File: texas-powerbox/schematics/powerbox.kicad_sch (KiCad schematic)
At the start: 32 parts, among them J1 BATTERY, J2 ADAPTER, J3 USB_STACKED, J4 USB_STACKED, J7 5V, J8 24V, K1 J107F1CS1224VDC.36, Q1 AOD417, U1 TPS54331GDR

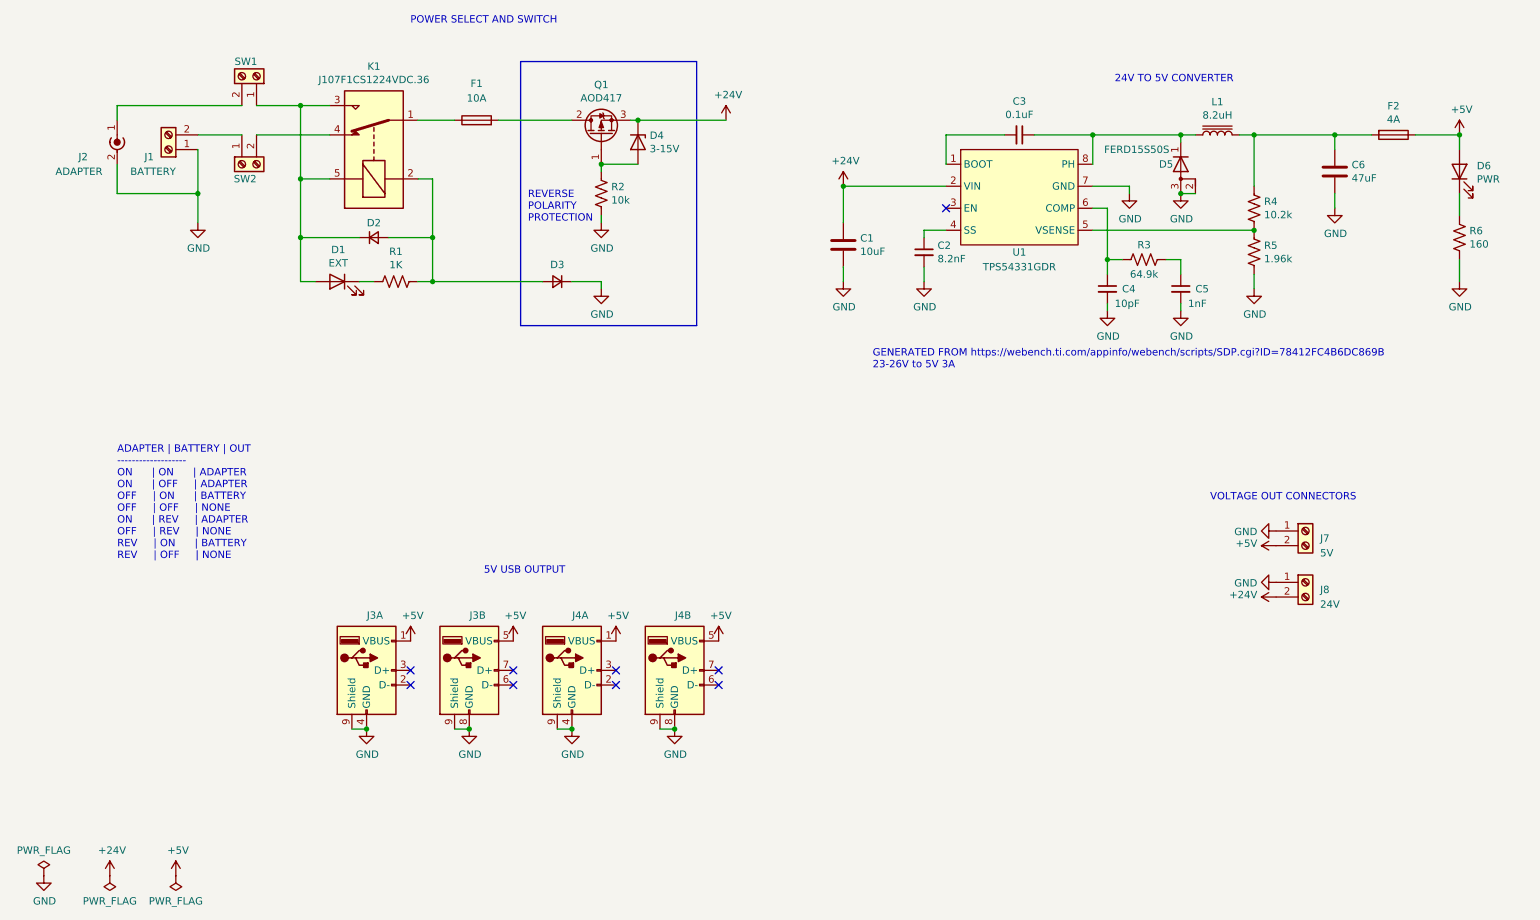
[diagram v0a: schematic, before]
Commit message: updated to use alternative bulk converter
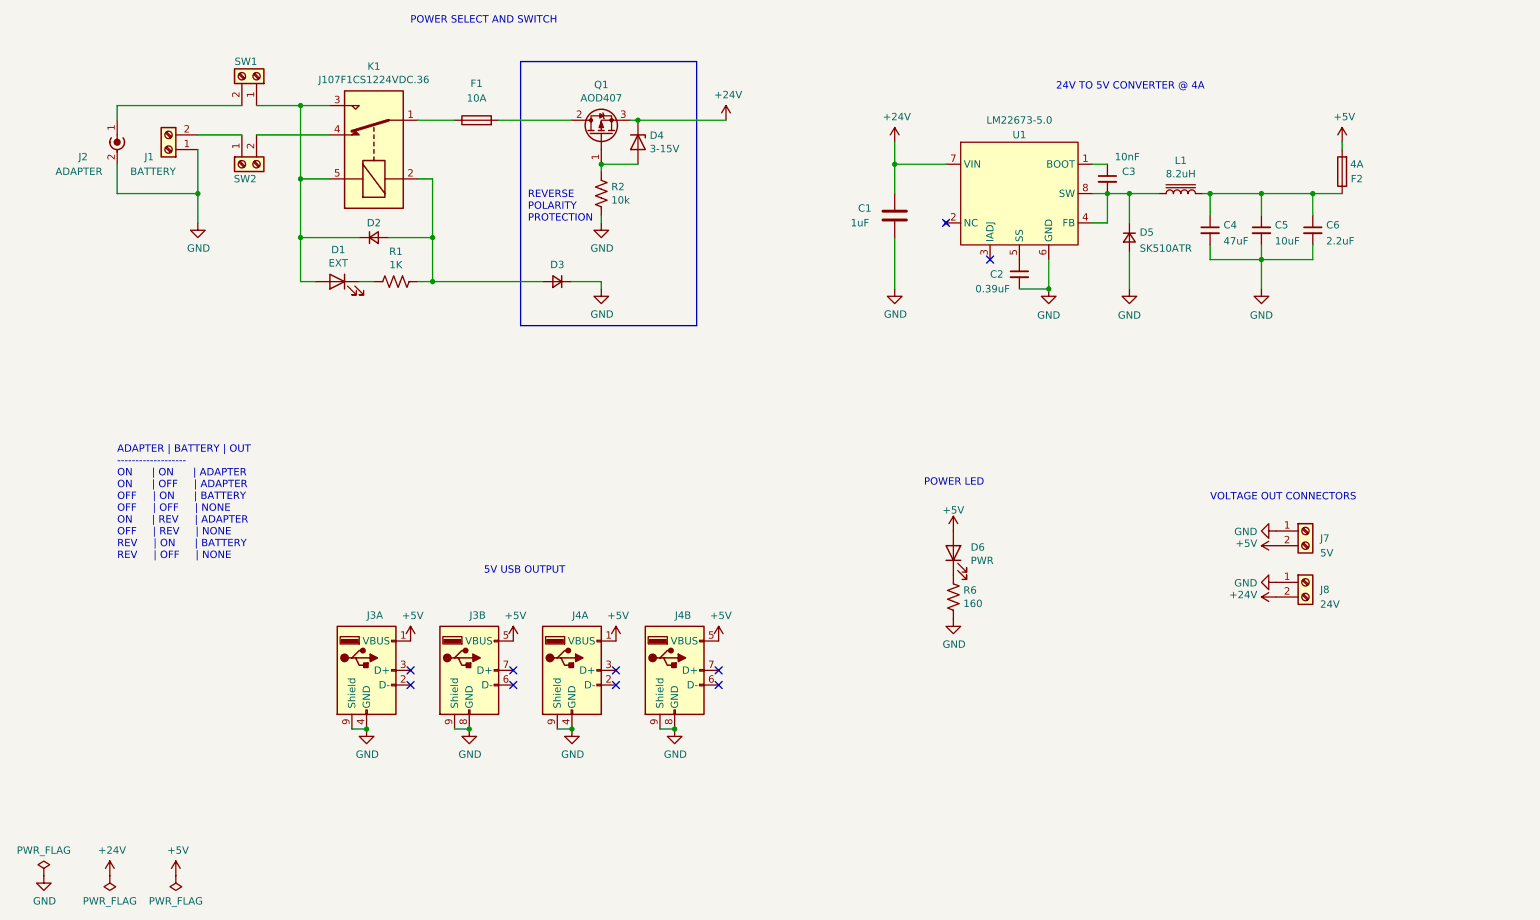
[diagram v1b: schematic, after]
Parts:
- removed C6: 47uF, Capacitor_SMD:C_0805_2012Metric_Pad1.18x1.45mm_HandSolder, symbol Device:C
- removed D5: FERD15S50S, Package_TO_SOT_SMD:TO-252-2, symbol Device:D_KAA
- removed R3: 64.9k, Resistor_SMD:R_0805_2012Metric_Pad1.20x1.40mm_HandSolder, symbol Device:R_US
- removed R4: 10.2k, Resistor_SMD:R_0805_2012Metric_Pad1.20x1.40mm_HandSolder, symbol Device:R_US
- removed R5: 1.96k, Resistor_SMD:R_0805_2012Metric_Pad1.20x1.40mm_HandSolder, symbol Device:R_US
- removed U1: TPS54331GDR, Package_SO:TI_SO-PowerPAD-8_ThermalVias, symbol powerbox:TPS54331GDR
- added C6: 2.2uF, Capacitor_SMD:C_0805_2012Metric_Pad1.18x1.45mm_HandSolder, symbol Device:C_Small
- added D5: SK510ATR, Diode_SMD:D_SMA_Handsoldering, symbol Device:D_Small
- added U1: LM22673-5.0, Package_SO:TI_SO-PowerPAD-8_ThermalVias, symbol powerbox:LM22673-5.0
- C1: value 10uF -> 1uF
- C2: value 8.2nF -> 0.39uF
- C3: value 0.1uF -> 10nF
- C4: value 10pF -> 47uF
- C5: value 1nF -> 10uF
- Q1: value AOD417 -> AOD407; footprint Package_TO_SOT_SMD:TO-252-2 -> Package_TO_SOT_SMD:TO-252-3
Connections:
- net +24V: now also U1.7 (VIN)
- net +5V: now also F2.2; no longer F2.1
- net GND: now also C6.2, D5.2 (A), U1.6 (GND)
- net at C3.2: now also L1.1, D5.1 (K), U1.4 (FB), U1.8 (SW)
- net at C2.1: now also U1.5 (SS)
- net at C4.1: now also C5.1, F2.1, L1.2, C6.1
- net at C3.1: now also U1.1 (BOOT); no longer L1.1
- no-connect marks 9 -> 10
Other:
- note added: "24V TO 5V CONVERTER @ 4A"
- note added: "POWER LED"
- note removed: "24V TO 5V CONVERTER"
- note removed: "GENERATED FROM https://webench.ti.com/appinfo/webench/scripts/SDP.cgi?ID=78412FC4B6DC869B 23-26V to 5V 3A"
- moved on the sheet: C1, D6, F2, L1, R6

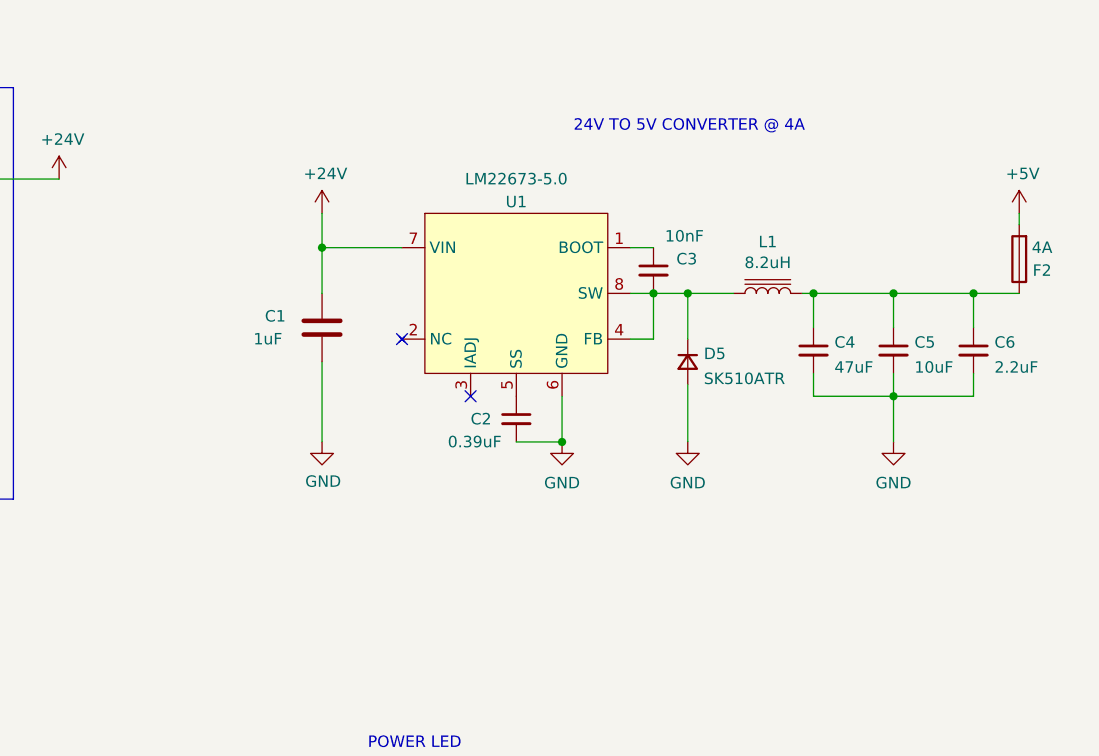
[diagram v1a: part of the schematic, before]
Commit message: update regulator input capacitor and add comment
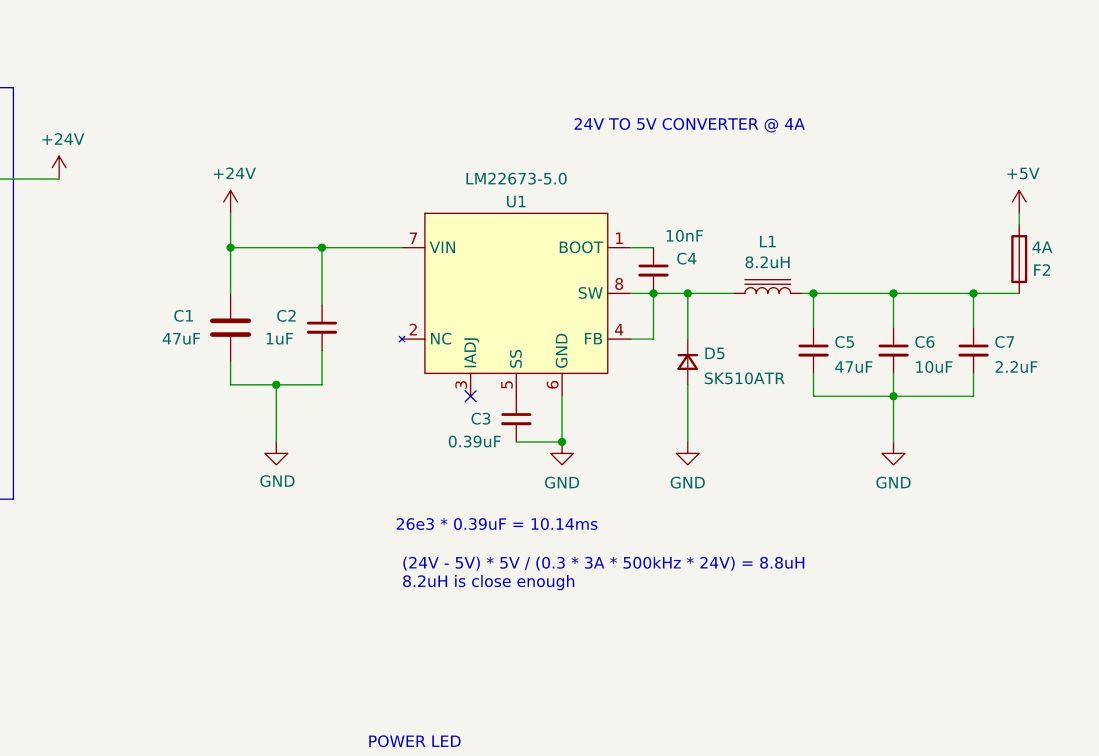
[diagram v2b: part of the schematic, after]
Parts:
- added C2: 1uF, Capacitor_SMD:C_0805_2012Metric_Pad1.18x1.45mm_HandSolder, symbol Device:C_Small
- C1: value 1uF -> 47uF
- renumbered C2 to C3, C3 to C4, C4 to C5, C5 to C6, C6 to C7
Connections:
- net +24V: now also C2.1
- net GND: now also C2.2
- no-connect marks 10 -> 9
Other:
- note added: "(24V - 5V) * 5V / (0.3 * 3A * 500kHz * 24V) = 8.8uH 8.2uH is close enough"
- note added: "26e3 * 0.39uF = 10.14ms"
- moved on the sheet: C1
